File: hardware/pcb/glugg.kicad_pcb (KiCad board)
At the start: 2 copper layers, 60 x 50 mm, 14 parts, among them J1 LED panel, U1 ESP32-S3-Zero, U2 ESP32-H2-Zero, U3 74HCT32

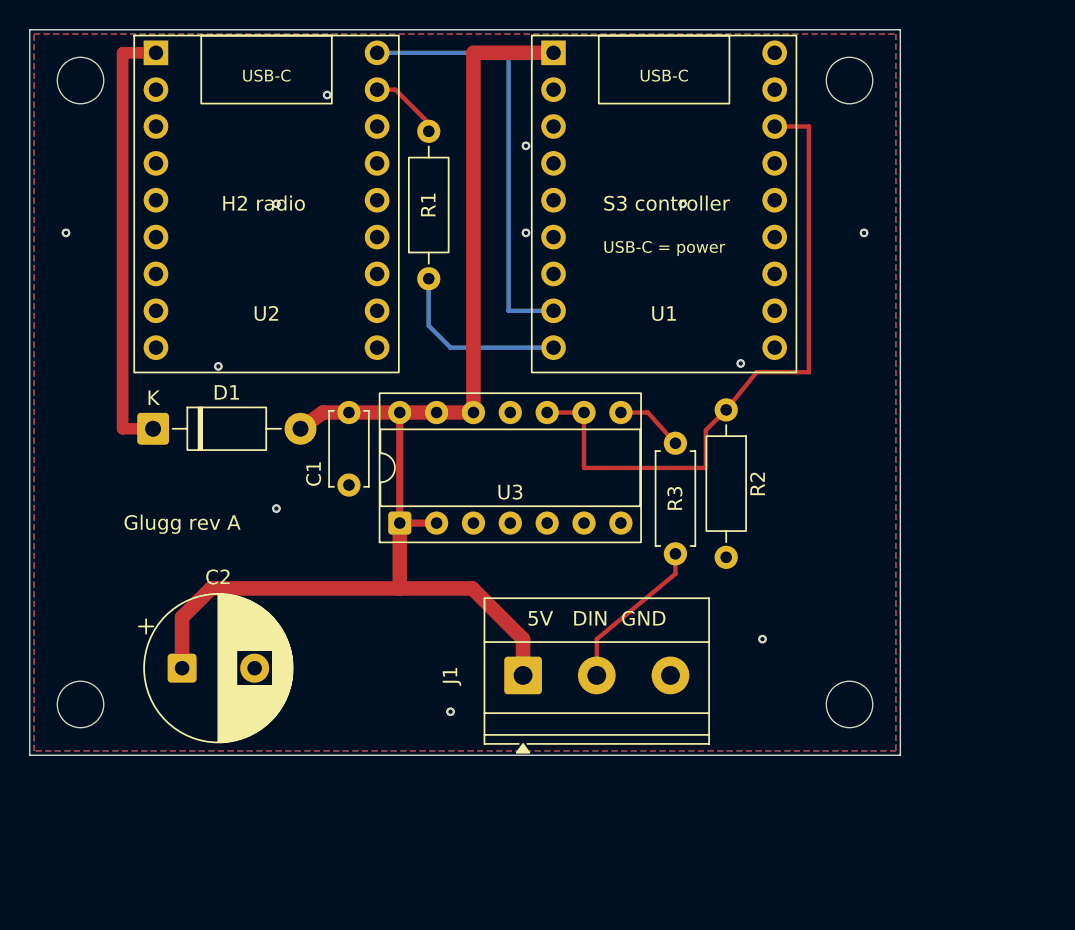
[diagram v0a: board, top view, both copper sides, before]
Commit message: PCB rev A: 5 mm margin and rounded corners
The board grows from 60 x 50 to 70 x 60 mm with a 5 mm margin round the
unchanged parts area, 3 mm rounded corners, and the M3 holes moved out to
3.5 mm from the corners. DRC with schematic parity is still clean. The
Gerber zip, renders and 1:1 print are regenerated.

Co-Authored-By: Claude Opus 5.5 <noreply@anthropic.com>
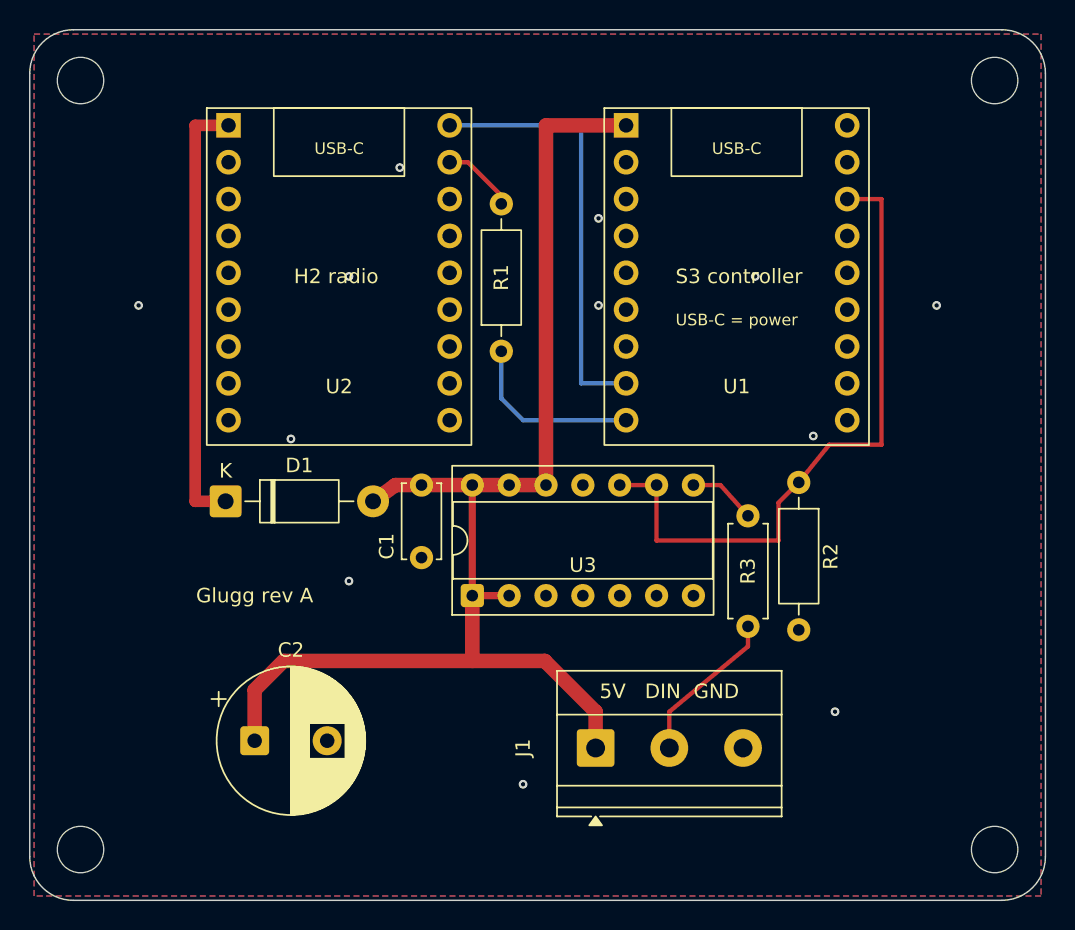
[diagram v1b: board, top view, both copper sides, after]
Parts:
- moved H4 14.1 mm to (166.5, 106.5)
- moved H2 10.0 mm to (166.5, 53.5)
- moved H3 10.0 mm to (103.5, 106.5)
- moved C1 7.07 mm to (127.0, 81.4)
- moved C2 7.07 mm to (115.5, 99.0)
- moved D1 7.07 mm to (113.5, 82.5)
- moved J1 7.07 mm to (139.0, 99.5)
- moved R1 7.07 mm to (132.5, 72.2)
- moved R2 7.07 mm to (153.0, 81.2)
- moved R3 7.07 mm to (149.5, 83.5)
- moved U1 7.07 mm to (141.1, 56.6)
- moved U2 7.07 mm to (113.7, 56.6)
- moved U3 7.07 mm to (130.5, 89.0)
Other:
- board size 60 x 50 mm -> 70 x 60 mm
